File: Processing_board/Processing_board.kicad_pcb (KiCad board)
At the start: 4 copper layers, 95.2 x 62 mm, 143 parts, among them J1 Conn_01x08_Pin, J10 CONMHF1-SMD-G-T, J11 USB4215-03-A_REVA, J12 Conn_01x02_Pin, J2 Conn_01x08_Pin, J3 Conn_01x06_Pin, J4 Conn_01x03_Pin, J5 Conn_01x03_Pin, J6 Conn_01x02_Pin, J8 Conn_01x03_Pin, J9 Conn_01x03_Pin, Q1 DMP3056LSS-13, Q2 DMN66D0LT-7, Q3 DMN66D0LT-7, SW1 TL3305BF100QG, SW2 TL3305BF100QG, U1 STM32WBA63CIU6, U10 ADS1299IPAG, U11 ADS1299IPAG, U5 LD1117S50TR_SOT223, U6 LD1117S33TR_SOT223, U8 BGS13SN8E6327XTSA1, U9 MCP2200-I_SO

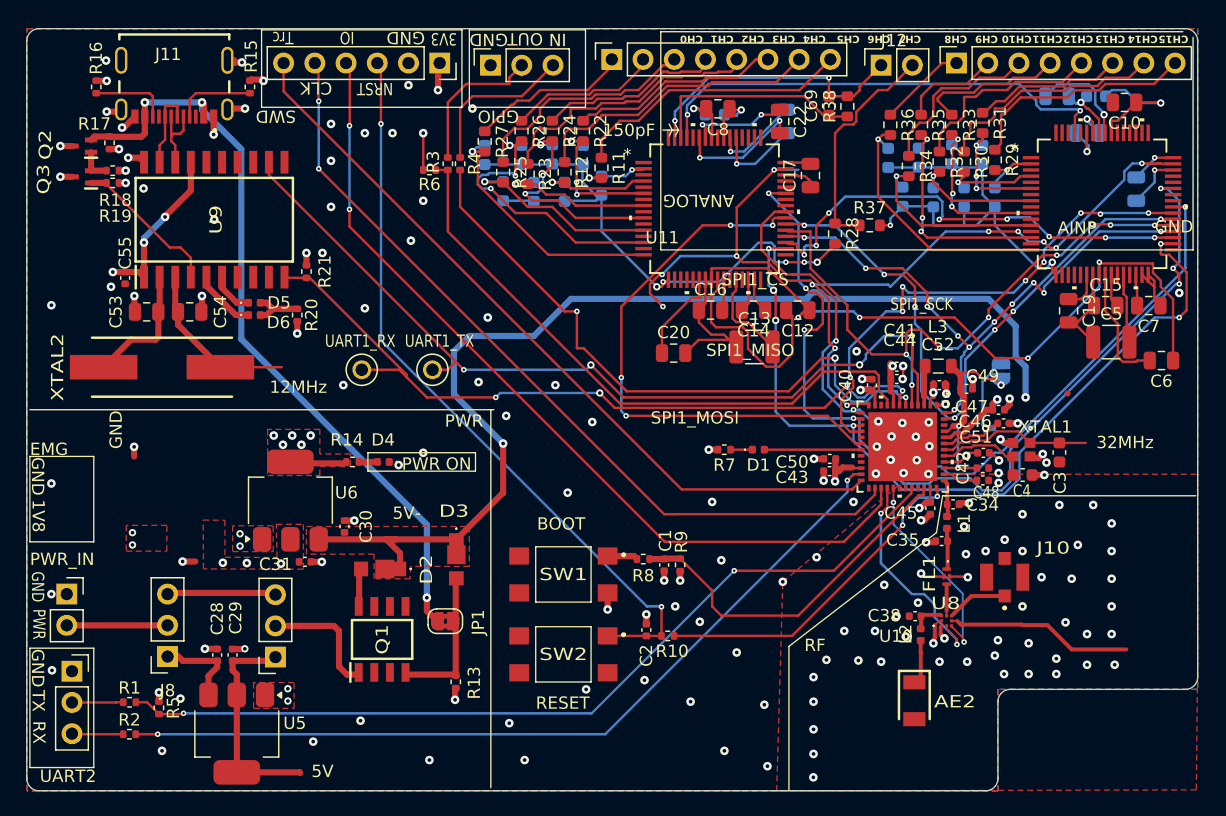
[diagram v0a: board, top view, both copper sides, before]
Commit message: Add the new power supply and connect the ADCs at the GND an power
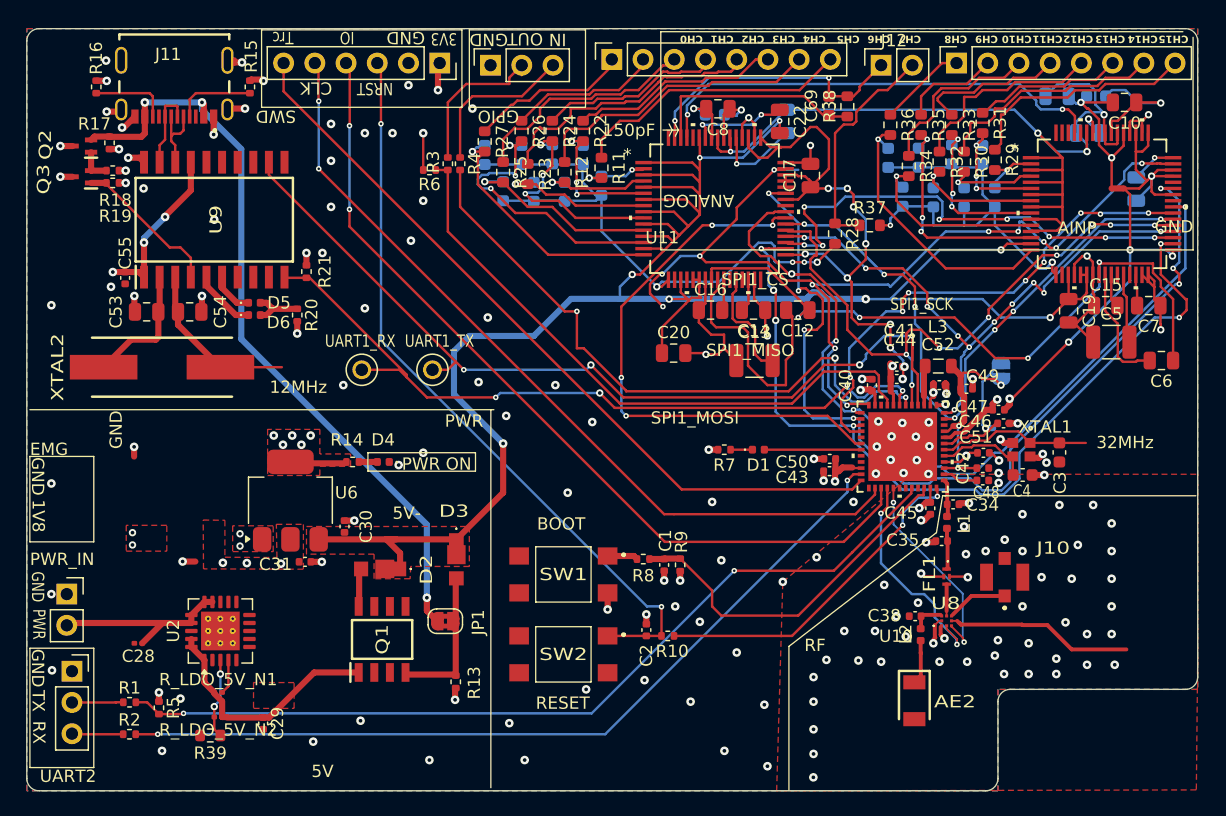
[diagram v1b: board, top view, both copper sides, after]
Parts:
- removed J8, J9: Conn_01x03_Pin, Connector_PinSocket_2.54mm:PinSocket_1x03_P2.54mm_Vertical
- removed U5: LD1117S50TR_SOT223, Package_TO_SOT_SMD:SOT-223-3_TabPin2
- added NT1: NetTie_2, NetTie:NetTie-2_SMD_Pad0.5mm, F.Cu at (167.5, 79.0)
- added R39: 27k, Resistor_SMD:R_0603_1608Metric, F.Cu at (93.7, 123.5)
- added R_LDO_5V_N1: 86.6k, Resistor_SMD:R_0201_0603Metric, F.Cu at (94.3, 120.0)
- added R_LDO_5V_N2: 249k, Resistor_SMD:R_0201_0603Metric, F.Cu at (94.3, 122.0)
- added U2: TPS7A7200RGW, Package_DFN_QFN:Texas_RGW0020A_VQFN-20-1EP_5x5mm_P0.65mm_EP3.15x3.15mm_ThermalVias, F.Cu at (94.5, 115.0)
- C28: value 100nF -> 100p; footprint Capacitor_SMD:C_0402_1005Metric -> Capacitor_SMD:C_0201_0603Metric
- C29: value 10uF -> 4.7u
- moved C28 6.49 mm to (87.8, 116.0), turned to 180 degrees
- moved C29 6.10 mm to (98.0, 122.5)
- moved C13 1.10 mm to (137.9, 93.0)
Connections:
- C17 pad 1: GNDD -> GND
- C17 pad 2: VDD -> +3.3V
- C18 pad 1: GNDD -> GND
- C18 pad 2: VDD -> +3.3V
- C19 pad 1: VDDA -> +5V
- C20 pad 1: VDDA -> +5V
- C21 pad 2: VDDA -> +5V
- C22 pad 2: VDDA -> +5V
- C23 pad 2: VDDA -> +5V
- C24 pad 2: VDDA -> +5V
- C28 pad 1: GND -> /Power
- C28 pad 2: /Power switching and voltage adaptation/Pre_LDO5V -> GND
- C29 pad 1: GND -> /Power switching and voltage adaptation/STABLE 5V
- C29 pad 2: /Power switching and voltage adaptation/Post_LDO5V -> GND
- Q1 pad 1: /Power switching and voltage adaptation/5V_Pre_PMOS -> /Power switching and voltage adaptation/STABLE 5V
- U10 pad 1: VDDA -> +5V
- U10 pad 11: VDDA -> +5V
- U10 pad 13: VDDA -> +5V
- U10 pad 15: VDDA -> +5V
- U10 pad 19: VDDA -> +5V
- U10 pad 21: VDDA -> +5V
- U10 pad 22: VDDA -> +5V
- U10 pad 3: VDDA -> +5V
- U10 pad 33: GNDD -> GND
- U10 pad 42: GNDD -> GND
- U10 pad 44: GNDD -> GND
- U10 pad 45: GNDD -> GND
- U10 pad 46: GNDD -> GND
- U10 pad 48: VDD -> +3.3V
- U10 pad 49: GNDD -> GND
- U10 pad 5: VDDA -> +5V
- U10 pad 50: VDD -> +3.3V
- U10 pad 51: GNDD -> GND
- U10 pad 52: VDD -> +3.3V
- U10 pad 54: VDDA -> +5V
- U10 pad 56: VDDA -> +5V
- U10 pad 59: VDDA -> +5V
- U10 pad 7: VDDA -> +5V
- U10 pad 9: VDDA -> +5V
- U11 pad 1: VDDA -> +5V
- U11 pad 11: VDDA -> +5V
- U11 pad 13: VDDA -> +5V
- U11 pad 15: VDDA -> +5V
- U11 pad 19: VDDA -> +5V
- U11 pad 21: VDDA -> +5V
- U11 pad 22: VDDA -> +5V
- U11 pad 3: VDDA -> +5V
- U11 pad 33: GNDD -> GND
- U11 pad 42: GNDD -> GND
- U11 pad 44: GNDD -> GND
- U11 pad 45: GNDD -> GND
- U11 pad 46: GNDD -> GND
- U11 pad 48: VDD -> +3.3V
- U11 pad 49: GNDD -> GND
- U11 pad 5: VDDA -> +5V
- U11 pad 50: VDD -> +3.3V
- U11 pad 51: GNDD -> GND
- U11 pad 52: VDD -> +3.3V
- U11 pad 54: VDDA -> +5V
- U11 pad 56: VDDA -> +5V
- U11 pad 59: VDDA -> +5V
- U11 pad 7: VDDA -> +5V
- U11 pad 9: VDDA -> +5V
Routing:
- net +5V: track 88.8 -> 254.3 mm, vias 2 -> 12
- net GND: track 43.3 -> 135.9 mm, vias 160 -> 166
- net VDDA: track 40.4 -> 0.00 mm, vias 5 -> 0
- net /Power switching and voltage adaptation/STABLE 5V: track 0.00 -> 20.0 mm
- net /Power switching and voltage adaptation/Post_LDO5V: track 17.9 -> 0.00 mm
- net GNDA: track 56.2 -> 73.8 mm, vias 6 -> 11
- net +3.3V: track 52.6 -> 67.0 mm, vias 27 -> 31
- net /Power switching and voltage adaptation/5V_Pre_PMOS: track 10.4 -> 0.00 mm
- net /Power: track 8.20 -> 17.7 mm
- net /Power switching and voltage adaptation/Skip_LDO5V: track 7.69 -> 0.00 mm
- net GNDD: track 7.35 -> 0.00 mm, vias 1 -> 0
- net Net-(U2-FB): track 0.00 -> 6.75 mm, vias 0 -> 2
- net /Power switching and voltage adaptation/Pre_LDO5V: track 6.59 -> 0.00 mm
- net VDD: track 5.64 -> 0.00 mm, vias 1 -> 0
- net Net-(U10-VREFN): track 16.7 -> 20.0 mm
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- added copper zone on In1.Cu, net GNDA
